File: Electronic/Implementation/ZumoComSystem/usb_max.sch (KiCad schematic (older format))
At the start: 2 parts, among them J2 USB_A, U5 MAX3421EEHJ+T

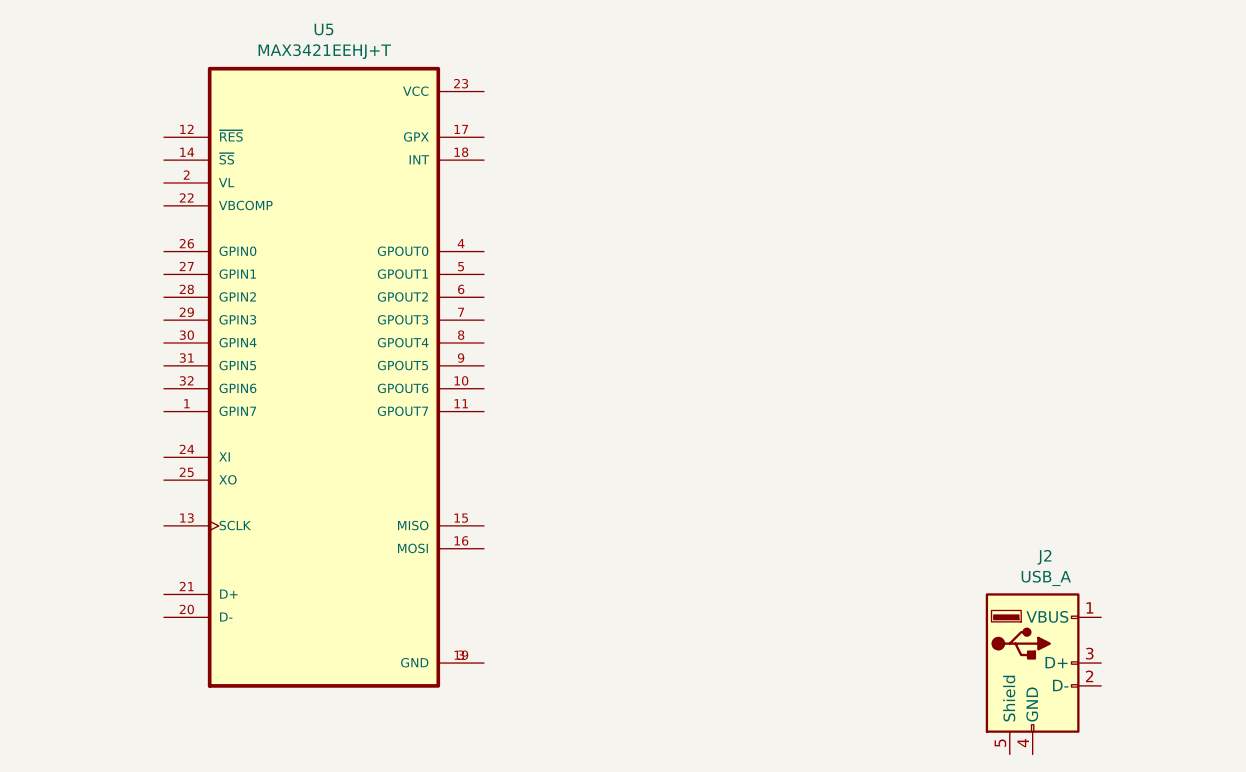
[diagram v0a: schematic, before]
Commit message: electronic -> Schematic -> add hierarchical pins, modified Regulator page
           -> BOM & Clac: add new inductors
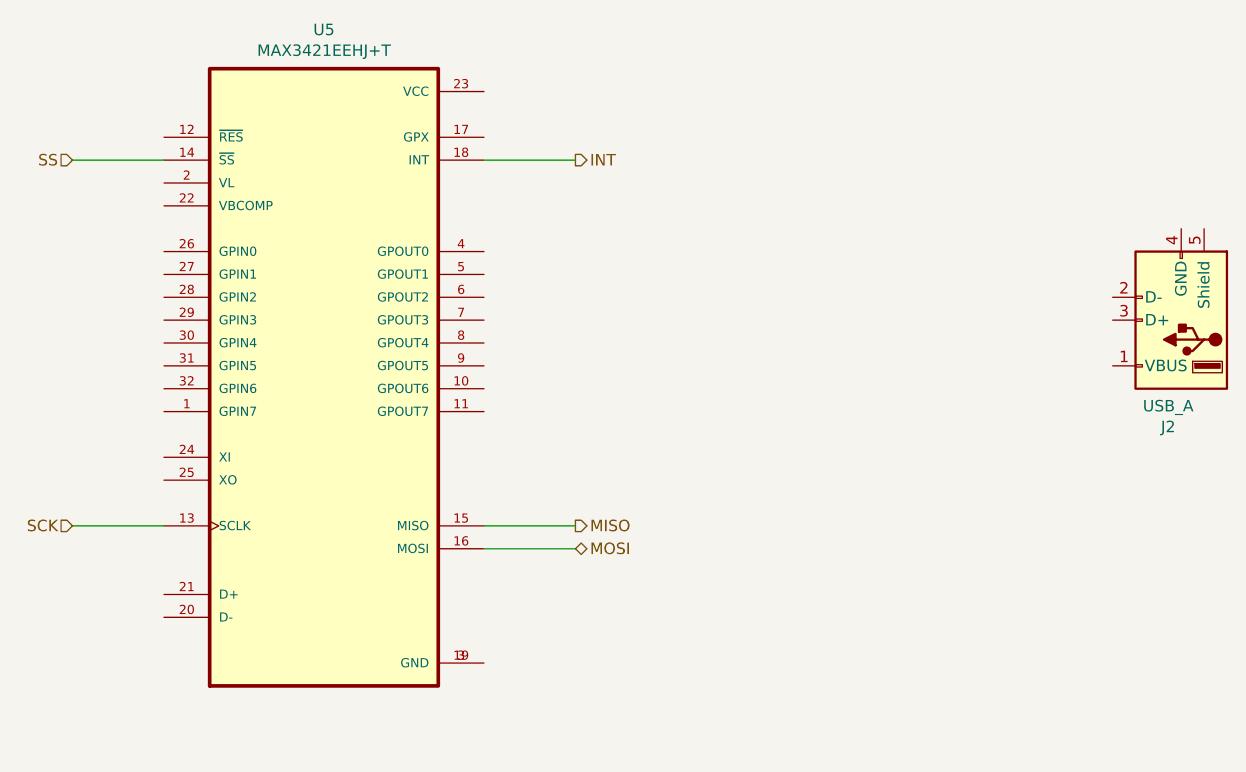
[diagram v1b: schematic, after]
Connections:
- net SCK: now reaches U5.13 (SCLK)
- net SS: now reaches U5.14 (~SS)
- net MISO: now reaches U5.15 (MISO)
- net MOSI: now reaches U5.16 (MOSI)
- net INT: now reaches U5.18 (INT)
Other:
- moved on the sheet: J2
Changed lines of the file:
@@
 L Connector:USB_A J?
 U 1 1 60C6499B
-P 8450 4250
+P 9100 2750
 AR Path="/60C6499B" Ref="J?"  Part="1"
 AR Path="/60C500E6/60C6499B" Ref="J2"  Part="1"
-F 0 "J2" H 8507 4717 50  0000 C CNN
-F 1 "USB_A" H 8507 4626 50  0000 C CNN
-F 2 "footprints:USB_A_Molex_105057_Vertical_2" H 8600 4200 50  0001 C CNN
-F 3 " ~" H 8600 4200 50  0001 C CNN
-	1    8450 4250
-	1    0    0    -1
+F 0 "J2" H 9157 3217 50  0000 C CNN
+F 1 "USB_A" H 9157 3126 50  0000 C CNN
+F 2 "footprints:USB_A_Molex_105057_Vertical_2" H 9250 2700 50  0001 C CNN
+F 3 " ~" H 9250 2700 50  0001 C CNN
+	1    9100 2750
+	-1   0    0    1
 $EndComp
 $Comp
@@
 F 1 "MAX3421EEHJ+T" H 5350 4329 50  0000 C CNN
 F 2 "QFP50P700X700X120-32N" H 5350 2950 50  0001 L BNN
-F 3 "" H 5350 2950 50  0001 L BNN
+F 3 "https://eu.mouser.com/datasheet/2/256/MAX3421E-1513231.pdf" H 5350 2950 50  0001 L BNN
 F 4 "Maxim Integrated" H 5350 2950 50  0001 L BNN "MF"
 F 5 "Ic Usb Periph/Host Cntrl 32tqfp - Max3421eehj+t" H 5350 2950 50  0001 L BNN "DESCRIPTION"
@@
 	1    0    0    -1
 $EndComp
+Text HLabel 4250 2050 0    50   Input ~ 0
+SS
+Text HLabel 6450 2050 2    50   Output ~ 0
+INT
+Text HLabel 4250 3650 0    50   Input ~ 0
+SCK
+Text HLabel 6450 3650 2    50   Output ~ 0
+MISO
+Text HLabel 6450 3750 2    50   BiDi ~ 0
+MOSI
+Wire Wire Line
+	4650 2050 4250 2050
+Wire Wire Line
+	6050 2050 6450 2050
+Wire Wire Line
+	4650 3650 4250 3650
+Wire Wire Line
+	6050 3650 6450 3650
+Wire Wire Line
+	6050 3750 6450 3750
 $EndSCHEMATC

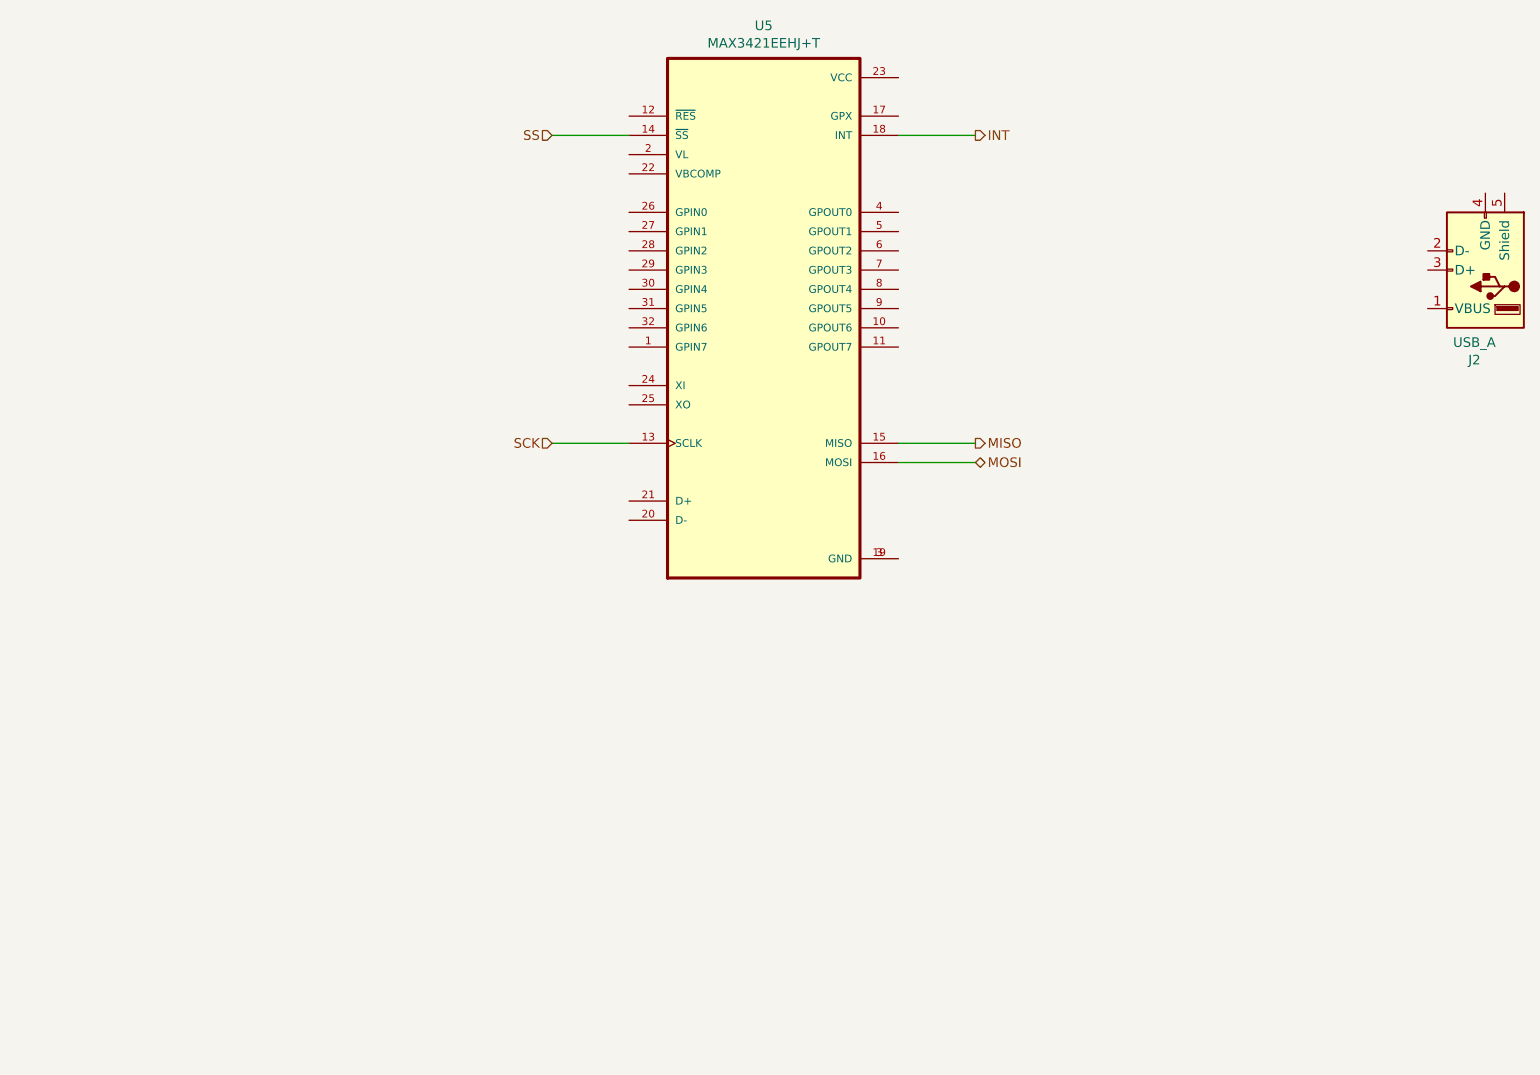
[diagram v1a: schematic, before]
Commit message: Electronic: Schematic: ESP I/Os, IF_Pololu Pins, USB_max
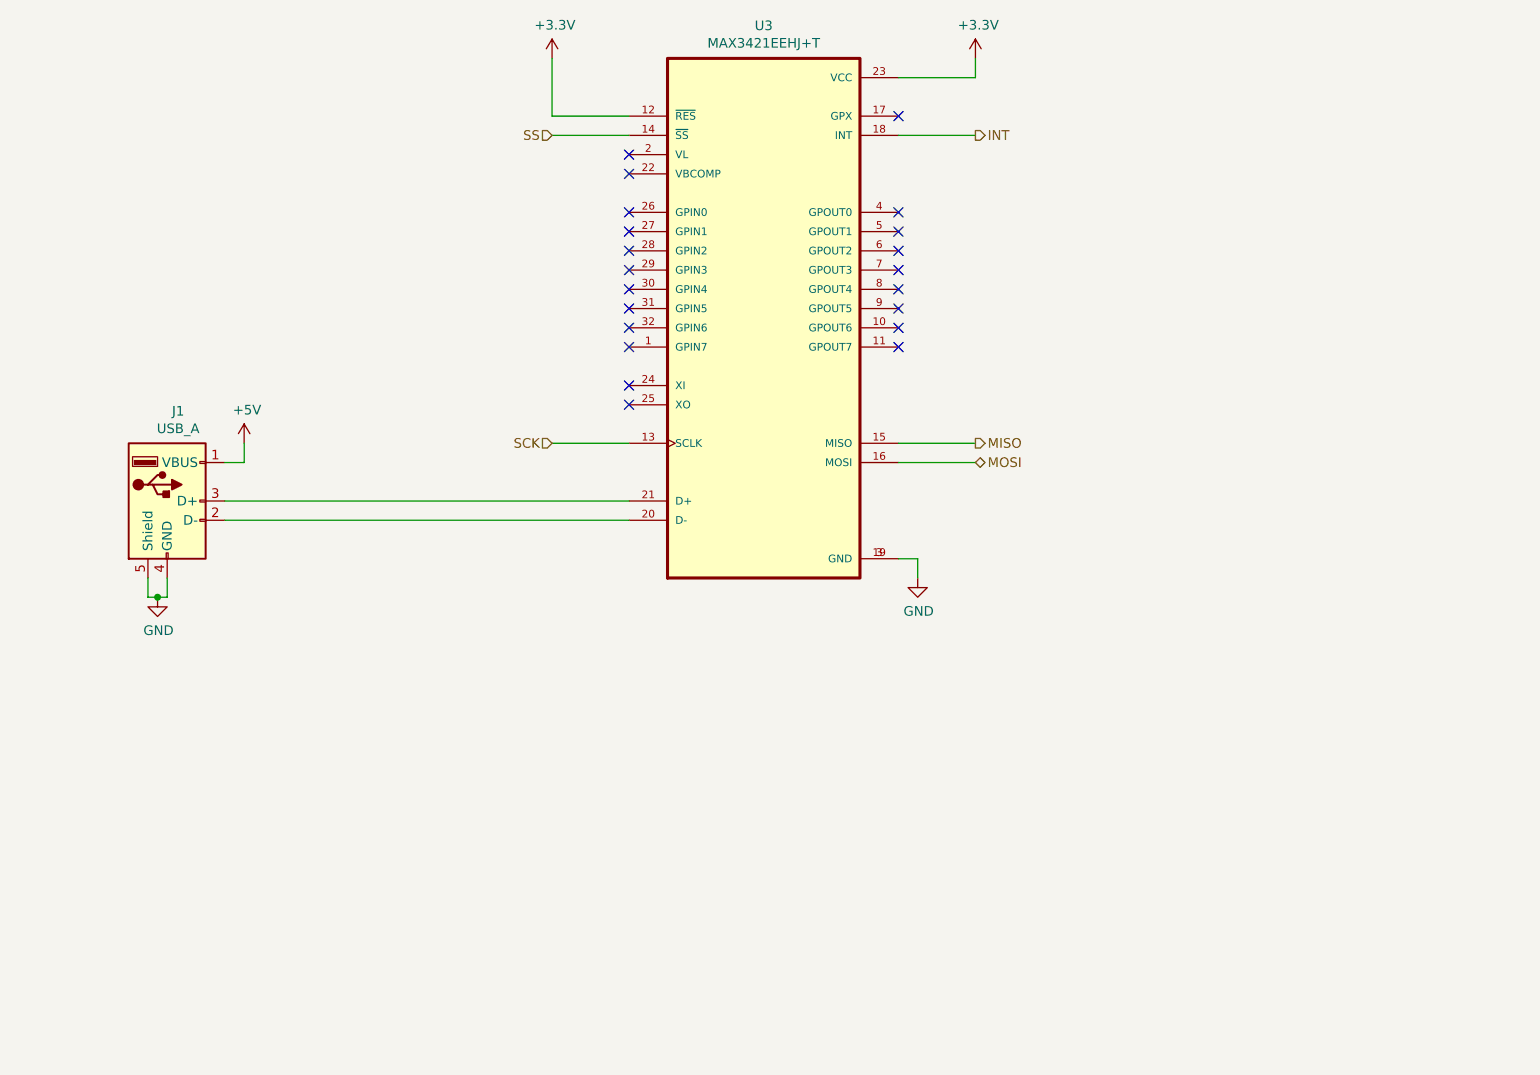
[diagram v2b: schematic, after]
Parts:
- renumbered J2 to J1, U5 to U3
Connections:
- net +5V: now reaches J1.1 (VBUS)
- net at J1.2 (D-): now also U3.20 (D-)
- net at J1.3 (D+): now also U3.21 (D+)
- net GND: now reaches J1.4 (GND)
- net GND: now also J1.5 (Shield), U3.19 (GND), U3.3 (GND)
- net +3V3: now reaches U3.12 (~RES)
- net +3V3: now also U3.23 (VCC)
- no-connect marks 0 -> 21
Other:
- moved on the sheet: J1
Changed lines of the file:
@@
 $Descr A4 11693 8268
 encoding utf-8
-Sheet 5 7
+Sheet 3 7
 Title "Zumo Communication System"
-Date "2021-06-11"
+Date "2021-07-28"
 Rev "V1.0"
 Comp "NewTec GmbH"
@@
 L Connector:USB_A J?
 U 1 1 60C6499B
-P 9100 2750
+P 2250 3950
 AR Path="/60C6499B" Ref="J?"  Part="1"
-AR Path="/60C500E6/60C6499B" Ref="J2"  Part="1"
-F 0 "J2" H 9157 3217 50  0000 C CNN
-F 1 "USB_A" H 9157 3126 50  0000 C CNN
-F 2 "footprints:USB_A_Molex_105057_Vertical_2" H 9250 2700 50  0001 C CNN
-F 3 " ~" H 9250 2700 50  0001 C CNN
-	1    9100 2750
-	-1   0    0    1
+AR Path="/60C500E6/60C6499B" Ref="J1"  Part="1"
+F 0 "J1" H 2307 4417 50  0000 C CNN
+F 1 "USB_A" H 2307 4326 50  0000 C CNN
+F 2 "footprints:USB_A_Molex_105057_Vertical_2" H 2400 3900 50  0001 C CNN
+F 3 " ~" H 2400 3900 50  0001 C CNN
+	1    2250 3950
+	1    0    0    -1
 $EndComp
 $Comp
-L MAX3421EEHJ_T:MAX3421EEHJ+T U5
+L MAX3421EEHJ_T:MAX3421EEHJ+T U3
 U 1 1 60C7A47F
 P 5350 2950
-F 0 "U5" H 5350 4420 50  0000 C CNN
+F 0 "U3" H 5350 4420 50  0000 C CNN
 F 1 "MAX3421EEHJ+T" H 5350 4329 50  0000 C CNN
 F 2 "QFP50P700X700X120-32N" H 5350 2950 50  0001 L BNN
@@
 Wire Wire Line
 	6050 3750 6450 3750
+Wire Wire Line
+	2550 3950 4650 3950
+Wire Wire Line
+	2550 4050 4650 4050
+Wire Wire Line
+	2250 4350 2250 4450
+Wire Wire Line
+	6050 4250 6150 4250
+Wire Wire Line
+	6150 4250 6150 4350
+Wire Wire Line
+	6050 1750 6450 1750
+Wire Wire Line
+	6450 1750 6450 1650
+Wire Wire Line
+	4650 1950 4250 1950
+$Comp
+L power:GND #PWR016
+U 1 1 6171550F
+P 6150 4350
+F 0 "#PWR016" H 6150 4100 50  0001 C CNN
+F 1 "GND" H 6155 4177 50  0000 C CNN
+F 2 "" H 6150 4350 50  0001 C CNN
+F 3 "" H 6150 4350 50  0001 C CNN
+	1    6150 4350
+	1    0    0    -1
+$EndComp
+$Comp
+L power:GND #PWR013
+U 1 1 617158D8
+P 2200 4450
+F 0 "#PWR013" H 2200 4200 50  0001 C CNN
+F 1 "GND" H 2205 4277 50  0000 C CNN
+F 2 "" H 2200 4450 50  0001 C CNN
+F 3 "" H 2200 4450 50  0001 C CNN
+	1    2200 4450
+	1    0    0    -1
+$EndComp
+Wire Wire Line
+	2150 4350 2150 4450
+Wire Wire Line
+	2150 4450 2200 4450
+Connection ~ 2200 4450
+Wire Wire Line
+	2200 4450 2250 4450
+Wire Wire Line
+	2550 3750 2650 3750
+Wire Wire Line
+	2650 3750 2650 3650
+$Comp
+L power:+5V #PWR014
+U 1 1 61716434
+P 2650 3650
+F 0 "#PWR014" H 2650 3500 50  0001 C CNN
+F 1 "+5V" H 2665 3823 50  0000 C CNN
+F 2 "" H 2650 3650 50  0001 C CNN
+F 3 "" H 2650 3650 50  0001 C CNN
+	1    2650 3650
+	1    0    0    -1
+$EndComp
+$Comp
+L power:+3.3V #PWR017
+U 1 1 61716978
+P 6450 1650
+F 0 "#PWR017" H 6450 1500 50  0001 C CNN
+F 1 "+3.3V" H 6465 1823 50  0000 C CNN
+F 2 "" H 6450 1650 50  0001 C CNN
+F 3 "" H 6450 1650 50  0001 C CNN
+	1    6450 1650
+	1    0    0    -1
+$EndComp
+$Comp
+L power:+3.3V #PWR015
+U 1 1 61716F75
+P 4250 1650
+F 0 "#PWR015" H 4250 1500 50  0001 C CNN
+F 1 "+3.3V" H 4265 1823 50  0000 C CNN
+F 2 "" H 4250 1650 50  0001 C CNN
+F 3 "" H 4250 1650 50  0001 C CNN
+	1    4250 1650
+	1    0    0    -1
+$EndComp
+Wire Wire Line
+	4250 1650 4250 1950
+NoConn ~ 4650 2150
+NoConn ~ 4650 2250
+NoConn ~ 4650 2450
+NoConn ~ 4650 2550
+NoConn ~ 4650 2650
+NoConn ~ 4650 2750
+NoConn ~ 4650 2850
+NoConn ~ 4650 2950
+NoConn ~ 4650 3050
+NoConn ~ 4650 3150
+NoConn ~ 4650 3350
+NoConn ~ 4650 3450
+NoConn ~ 6050 1950
+NoConn ~ 6050 2450
+NoConn ~ 6050 2550
+NoConn ~ 6050 2650
+NoConn ~ 6050 2750
+NoConn ~ 6050 2850
+NoConn ~ 6050 2950
+NoConn ~ 6050 3050
+NoConn ~ 6050 3150
 $EndSCHEMATC

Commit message: Electronic: no charger, added Cp2102 instead of Ft232, first palcement
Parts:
- added C7, C8: 18p, Capacitor_SMD:C_0603_1608Metric_Pad1.05x0.95mm_HandSolder, symbol Device:C
- added Y1: Crystal_GND24, Crystal:Crystal_SMD_3225-4Pin_3.2x2.5mm_HandSoldering, symbol Device:Crystal_GND24
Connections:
- net GND: now also C7.2, C8.2, Y1.2, Y1.4
- net D-: now reaches J1.2 (D-), U3.20 (D-)
- net D+: now reaches J1.3 (D+), U3.21 (D+)
- net XI: now reaches U3.24 (XI)
- net XI: now also C8.1, Y1.3
- net XO: now reaches U3.25 (XO)
- net XO: now also C7.1, Y1.1
- no-connect marks 21 -> 19
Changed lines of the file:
@@
 Sheet 3 7
 Title "Zumo Communication System"
-Date "2021-08-20"
+Date "2022-03-08"
 Rev "V1.0"
 Comp "NewTec GmbH"
@@
 	4650 1950 4250 1950
 $Comp
-L power:GND #PWR016
+L power:GND #PWR021
 U 1 1 6171550F
 P 6150 4350
-F 0 "#PWR016" H 6150 4100 50  0001 C CNN
+F 0 "#PWR021" H 6150 4100 50  0001 C CNN
 F 1 "GND" H 6155 4177 50  0000 C CNN
 F 2 "" H 6150 4350 50  0001 C CNN
@@
 $EndComp
 $Comp
-L power:GND #PWR013
+L power:GND #PWR015
 U 1 1 617158D8
 P 2200 4450
-F 0 "#PWR013" H 2200 4200 50  0001 C CNN
+F 0 "#PWR015" H 2200 4200 50  0001 C CNN
 F 1 "GND" H 2205 4277 50  0000 C CNN
 F 2 "" H 2200 4450 50  0001 C CNN
@@
 	2650 3750 2650 3650
 $Comp
-L power:+5V #PWR014
+L power:+5V #PWR017
 U 1 1 61716434
 P 2650 3650
-F 0 "#PWR014" H 2650 3500 50  0001 C CNN
+F 0 "#PWR017" H 2650 3500 50  0001 C CNN
 F 1 "+5V" H 2665 3823 50  0000 C CNN
 F 2 "" H 2650 3650 50  0001 C CNN
@@
 $EndComp
 $Comp
-L power:+3.3V #PWR017
+L power:+3.3V #PWR022
 U 1 1 61716978
 P 6450 1650
-F 0 "#PWR017" H 6450 1500 50  0001 C CNN
+F 0 "#PWR022" H 6450 1500 50  0001 C CNN
 F 1 "+3.3V" H 6465 1823 50  0000 C CNN
 F 2 "" H 6450 1650 50  0001 C CNN
@@
 $EndComp
 $Comp
-L power:+3.3V #PWR015
+L power:+3.3V #PWR020
 U 1 1 61716F75
 P 4250 1650
-F 0 "#PWR015" H 4250 1500 50  0001 C CNN
+F 0 "#PWR020" H 4250 1500 50  0001 C CNN
 F 1 "+3.3V" H 4265 1823 50  0000 C CNN
 F 2 "" H 4250 1650 50  0001 C CNN
@@
 NoConn ~ 4650 3050
 NoConn ~ 4650 3150
-NoConn ~ 4650 3350
-NoConn ~ 4650 3450
 NoConn ~ 6050 1950
 NoConn ~ 6050 2450
@@
 NoConn ~ 6050 3050
 NoConn ~ 6050 3150
+$Comp
+L Device:C C7
+U 1 1 623D76FD
+P 1550 6350
+F 0 "C7" H 1665 6396 50  0000 L CNN
+F 1 "18p" H 1665 6305 50  0000 L CNN
+F 2 "Capacitor_SMD:C_0603_1608Metric_Pad1.05x0.95mm_HandSolder" H 1588 6200 50  0001 C CNN
+F 3 "~" H 1550 6350 50  0001 C CNN
+	1    1550 6350
+	1    0    0    -1
+$EndComp
+$Comp
+L Device:C C8
+U 1 1 623D7CDF
+P 3000 6350
+F 0 "C8" H 3115 6396 50  0000 L CNN
+F 1 "18p" H 3115 6305 50  0000 L CNN
+F 2 "Capacitor_SMD:C_0603_1608Metric_Pad1.05x0.95mm_HandSolder" H 3038 6200 50  0001 C CNN
+F 3 "~" H 3000 6350 50  0001 C CNN
+	1    3000 6350
+	1    0    0    -1
+$EndComp
+$Comp
+L power:GND #PWR014
+U 1 1 623D7F8C
+P 1550 6500
+F 0 "#PWR014" H 1550 6250 50  0001 C CNN
+F 1 "GND" H 1555 6327 50  0000 C CNN
+F 2 "" H 1550 6500 50  0001 C CNN
+F 3 "" H 1550 6500 50  0001 C CNN
+	1    1550 6500
+	1    0    0    -1
+$EndComp
+$Comp
+L power:GND #PWR019
+U 1 1 623D8337
+P 3000 6500
+F 0 "#PWR019" H 3000 6250 50  0001 C CNN
+F 1 "GND" H 3005 6327 50  0000 C CNN
+F 2 "" H 3000 6500 50  0001 C CNN
+F 3 "" H 3000 6500 50  0001 C CNN
+	1    3000 6500
+	1    0    0    -1
+$EndComp
+Wire Wire Line
+	3000 5950 3000 6200
+Wire Wire Line
+	1550 5950 2100 5950
+Wire Wire Line
+	2400 5950 3000 5950
+Wire Wire Line
+	1550 5300 3500 5300
+Text Label 3500 5300 2    50   ~ 0
+XO
+Text Label 3500 5400 2    50   ~ 0
+XI
+Wire Wire Line
+	3000 5950 3000 5400
+Wire Wire Line
+	3000 5400 3500 5400
+Connection ~ 3000 5950
+Text Label 3200 3950 0    50   ~ 0
+D+
+Text Label 3200 4050 0    50   ~ 0
+D-
+Text Label 4050 3350 0    50   ~ 0
+XI
+Wire Wire Line
+	4650 3350 4050 3350
+Text Label 4050 3450 0    50   ~ 0
+XO
+Wire Wire Line
+	4050 3450 4650 3450
+$Comp
+L Device:Crystal_GND24 Y1
+U 1 1 623EF4A9
+P 2250 5950
+F 0 "Y1" H 2444 5996 50  0000 L CNN
+F 1 "Crystal_GND24" H 2000 5100 50  0000 L CNN
+F 2 "Crystal:Crystal_SMD_3225-4Pin_3.2x2.5mm_HandSoldering" H 2250 5950 50  0001 C CNN
+F 3 "https://www.diodes.com/assets/Datasheets/FL.pdf" H 2250 5950 50  0001 C CNN
+	1    2250 5950
+	1    0    0    -1
+$EndComp
+Wire Wire Line
+	1550 5300 1550 5950
+Wire Wire Line
+	2250 5750 2250 5500
+Wire Wire Line
+	2250 5500 2650 5500
+$Comp
+L power:GND #PWR018
+U 1 1 623F4A4F
+P 2650 5500
+F 0 "#PWR018" H 2650 5250 50  0001 C CNN
+F 1 "GND" H 2655 5327 50  0000 C CNN
+F 2 "" H 2650 5500 50  0001 C CNN
+F 3 "" H 2650 5500 50  0001 C CNN
+	1    2650 5500
+	1    0    0    -1
+$EndComp
+$Comp
+L power:GND #PWR016
+U 1 1 623F4CEC
+P 2250 6500
+F 0 "#PWR016" H 2250 6250 50  0001 C CNN
+F 1 "GND" H 2255 6327 50  0000 C CNN
+F 2 "" H 2250 6500 50  0001 C CNN
+F 3 "" H 2250 6500 50  0001 C CNN
+	1    2250 6500
+	1    0    0    -1
+$EndComp
+Wire Wire Line
+	2250 6150 2250 6500
+Connection ~ 1550 5950
+Wire Wire Line
+	1550 5950 1550 6200
 $EndSCHEMATC
